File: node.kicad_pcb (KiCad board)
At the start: 2 copper layers, 46 x 39 mm, 38 parts, among them J1 USB_B_Mini, J2 TC2030_NL, J3 FFC-0.5MM-6POS, J4 Port_1, J5 Port_2, J6 FFC-0.5MM-6POS, J7 Port_3, J8 Port_4, U1 PMIC-LDO-XC6204B332MR_SOT23-5_, U2 LP2985-5.0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

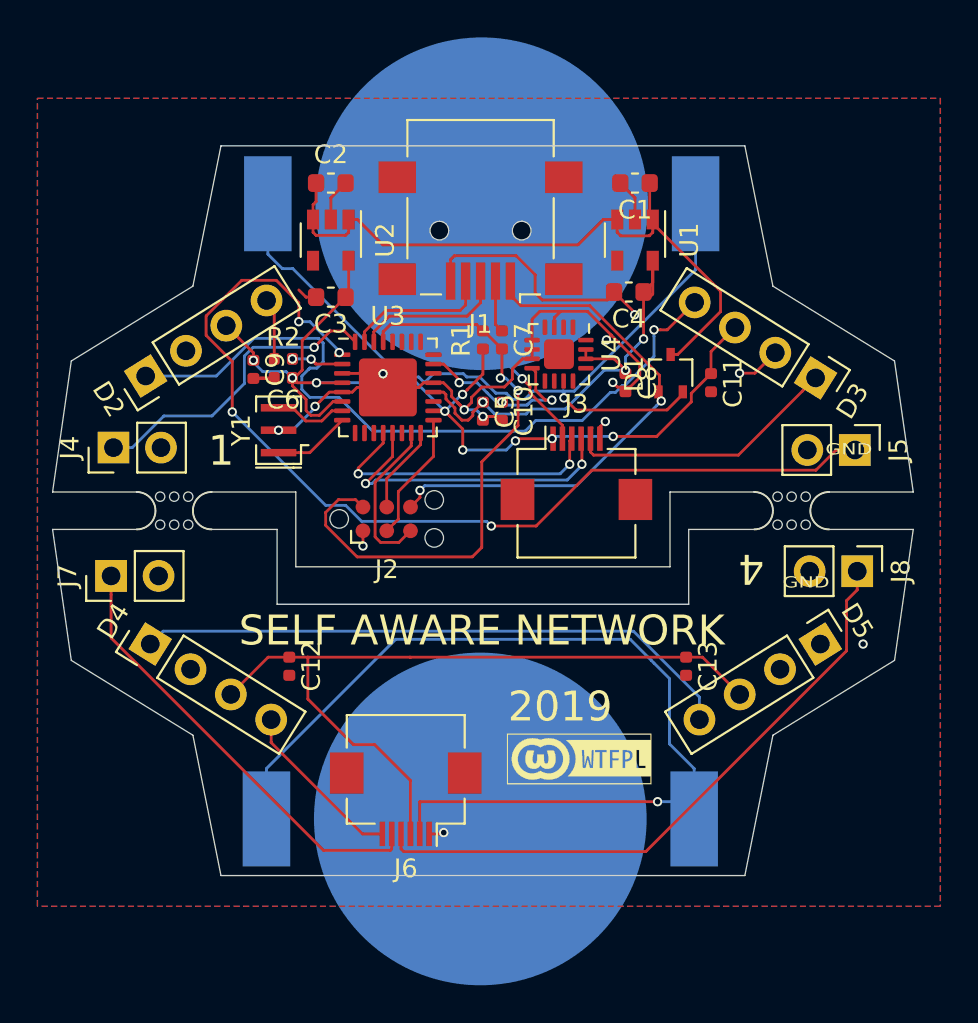
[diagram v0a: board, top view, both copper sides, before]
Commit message: Switch to small mouse-bite
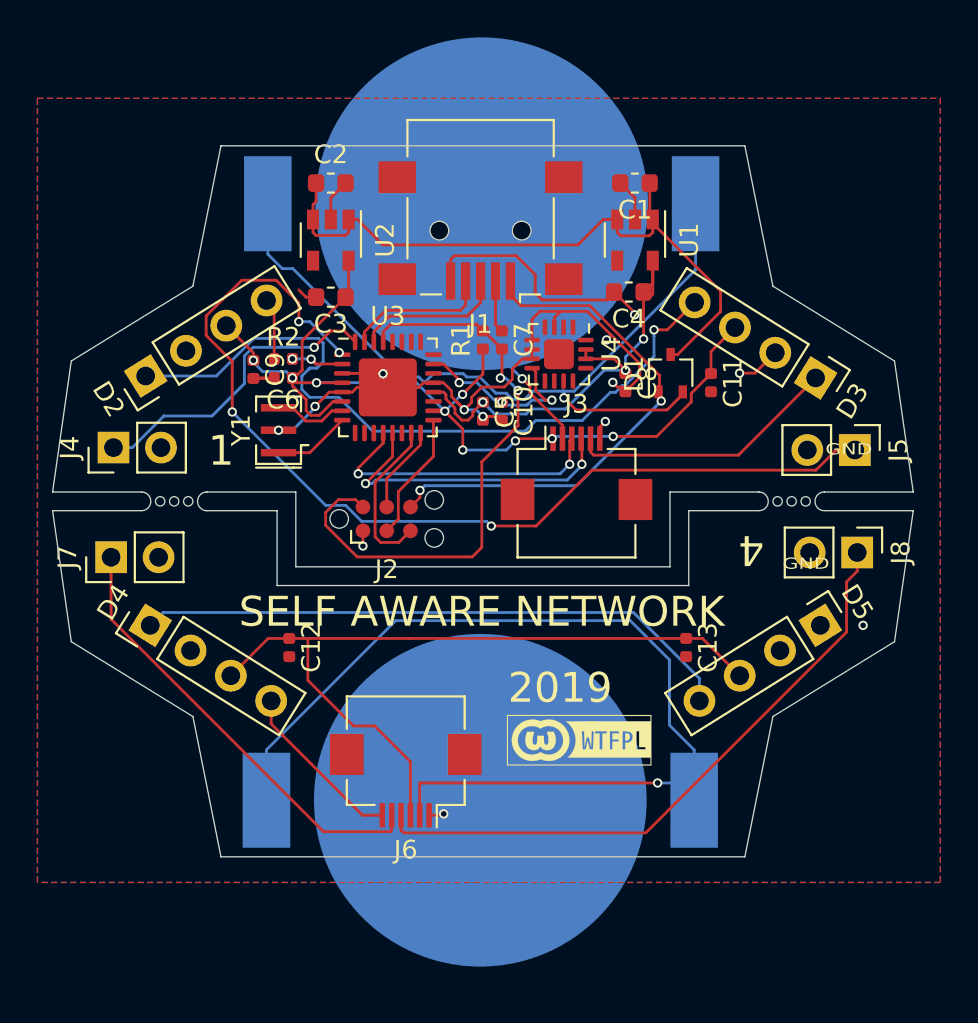
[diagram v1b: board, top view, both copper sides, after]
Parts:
- removed mouse-bite-2mm-slot (x2): VAL**, Panelization:mouse-bite-2mm-slot
- added mouse-bite: VAL**, node:mouse-bite, F.Cu at (163.5, 82.5)
- added mouse-bite: VAL**, node:mouse-bite, F.Cu at (130.5, 82.5)
- moved BT2 1.00 mm to (146.9, 98.5)
- moved C12 1.00 mm to (136.7, 90.3)
- moved C13 1.00 mm to (157.9, 90.3)
- moved D4 1.00 mm to (129.2, 89.1)
- moved D5 1.00 mm to (165.0, 89.1)
- moved G*** 1.00 mm to (152.1, 95.3)
- moved J6 1.00 mm to (142.9, 97.4)
- moved J7 1.00 mm to (127.1, 85.5)
- moved J8 1.00 mm to (167.0, 85.2)
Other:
- board size 46 x 39 mm -> 46 x 38 mm

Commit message: Fix: critically small features in license logo
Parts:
- moved G*** 2.78 mm to (152.5, 92.5)

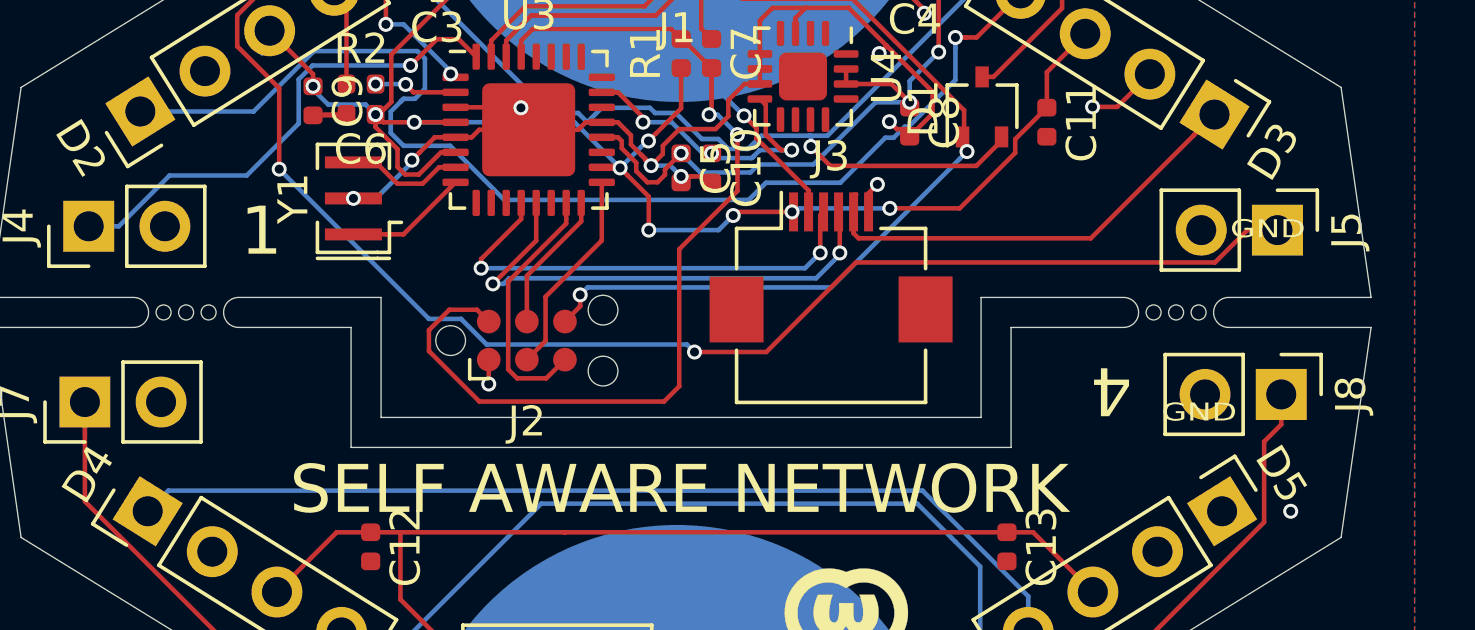
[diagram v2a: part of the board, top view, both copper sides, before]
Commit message: Annotate GND for ports
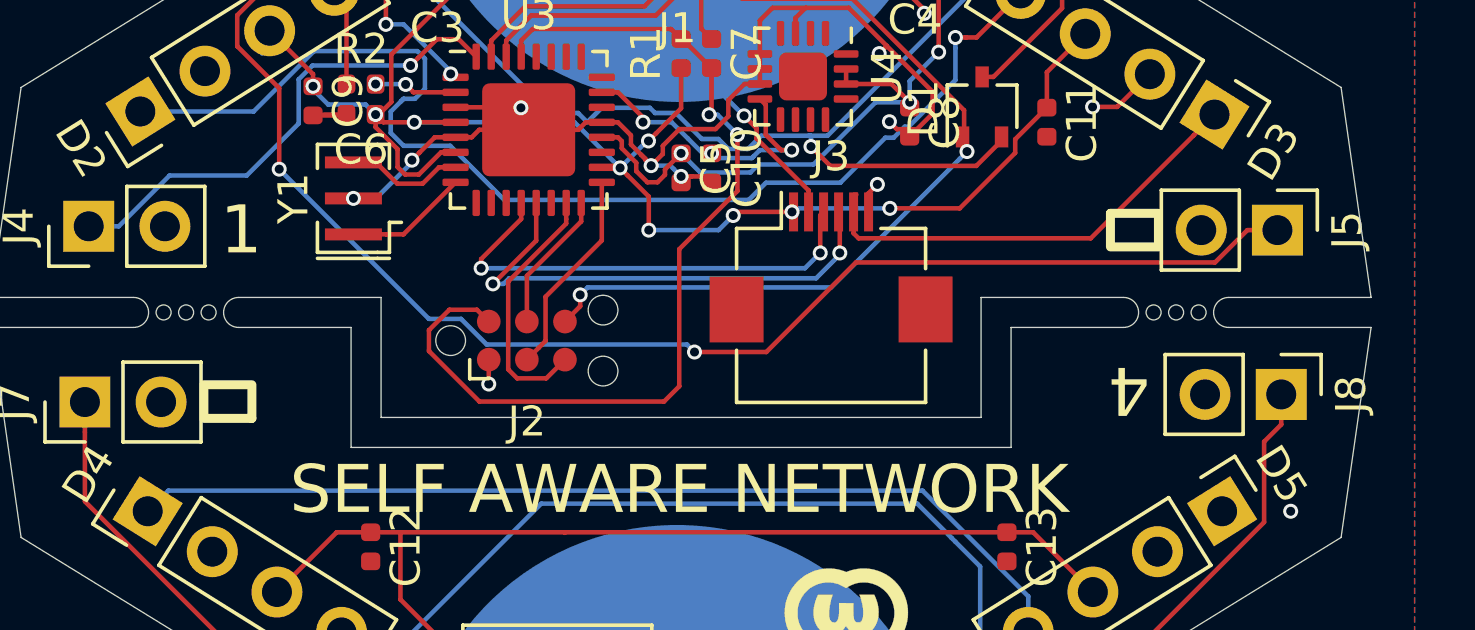
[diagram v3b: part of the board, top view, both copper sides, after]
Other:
- board text added: "⏚"
- board text removed: "GND"
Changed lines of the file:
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@@
   (general
     (thickness 1)
-    (drawings 117)
+    (drawings 119)
     (tracks 482)
     (zones 0)
@@
   (layers
     (0 F.Cu signal)
-    (31 B.Cu signal hide)
-    (32 B.Adhes user hide)
-    (33 F.Adhes user hide)
-    (34 B.Paste user hide)
+    (31 B.Cu signal)
+    (32 B.Adhes user)
+    (33 F.Adhes user)
+    (34 B.Paste user)
     (35 F.Paste user)
-    (36 B.SilkS user hide)
+    (36 B.SilkS user)
     (37 F.SilkS user)
-    (38 B.Mask user hide)
+    (38 B.Mask user)
     (39 F.Mask user)
-    (40 Dwgs.User user hide)
-    (41 Cmts.User user hide)
-    (42 Eco1.User user hide)
-    (43 Eco2.User user hide)
+    (40 Dwgs.User user)
+    (41 Cmts.User user)
+    (42 Eco1.User user)
+    (43 Eco2.User user)
     (44 Edge.Cuts user)
-    (45 Margin user hide)
-    (46 B.CrtYd user hide)
+    (45 Margin user)
+    (46 B.CrtYd user)
     (47 F.CrtYd user)
-    (48 B.Fab user hide)
+    (48 B.Fab user)
     (49 F.Fab user)
   )
@@
     (solder_mask_min_width 0.25)
     (aux_axis_origin 0 0)
-    (visible_elements 7FFFFF9F)
+    (visible_elements 7FFFFFBF)
     (pcbplotparams
       (layerselection 0x010fc_ffffffff)
@@
       (net 3 GND))
   )
+  (gr_text ⏚ (at 132.08 79.629 90) (layer B.SilkS)
+    (effects (font (size 1.6 1.6) (thickness 0.3)))
+  )
+  (gr_text ⏚ (at 162.179 85.217 270) (layer B.SilkS)
+    (effects (font (size 1.6 1.6) (thickness 0.3)))
+  )
+  (gr_text ⏚ (at 162.052 79.756 270) (layer F.SilkS)
+    (effects (font (size 1.6 1.6) (thickness 0.3)))
+  )
+  (gr_text ⏚ (at 131.953 85.471 90) (layer F.SilkS)
+    (effects (font (size 1.6 1.6) (thickness 0.3)))
+  )
   (gr_arc (start 165.25 82.5) (end 165.25 82) (angle -180) (layer Edge.Cuts) (width 0.0254))
   (gr_arc (start 161.75 82.5) (end 161.75 83) (angle -180) (layer Edge.Cuts) (width 0.0254))
@@
     (effects (font (size 1.6 1.6) (thickness 0.3)))
   )
-  (gr_text 4 (at 161.3408 85.10092 180) (layer F.SilkS)
+  (gr_text 4 (at 161.925 85.09 180) (layer F.SilkS)
     (effects (font (size 1.6 1.6) (thickness 0.3)))
   )
-  (gr_text 3 (at 132.842 85.36 180) (layer B.SilkS)
+  (gr_text 3 (at 132.334 85.344 180) (layer B.SilkS)
     (effects (font (size 1.6 1.6) (thickness 0.3)) (justify mirror))
   )
-  (gr_text 2 (at 161.417 79.756) (layer B.SilkS)
+  (gr_text 2 (at 161.798 79.756) (layer B.SilkS)
     (effects (font (size 1.6 1.6) (thickness 0.3)) (justify mirror))
   )
-  (gr_text 1 (at 133.0071 79.80172) (layer F.SilkS)
+  (gr_text 1 (at 132.334 79.756) (layer F.SilkS)
     (effects (font (size 1.6 1.6) (thickness 0.3)))
   )
@@
   (gr_line (start 133.60317 70.131025) (end 133.177341 70.393074) (layer Dwgs.User) (width 0.2))
   (gr_line (start 135.478784 72.205796) (end 135.216735 71.779966) (layer Dwgs.User) (width 0.2))
-  (gr_text GND (at 166.558 79.714) (layer F.SilkS)
-    (effects (font (size 0.6 0.8) (thickness 0.12)))
-  )
-  (gr_text GND (at 164.272 85.826) (layer F.SilkS)
-    (effects (font (size 0.6 0.8) (thickness 0.12)))
-  )
   (segment (start 157.683 76.521953) (end 157.698104 76.537057) (width 0.1524) (layer F.Cu) (net 1) (status 30))
   (segment (start 158.3665 70.1255) (end 158.3665 69.2873) (width 0.1524) (layer B.Cu) (net 1))
